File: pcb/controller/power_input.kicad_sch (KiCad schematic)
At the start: 8 parts, among them J3 USB_C_Receptacle_USB2.0_16P, U2 CH224K, U3 TPS54531DDAR

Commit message: cleaned up
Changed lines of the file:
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@@
 	(hierarchical_label "+5V"
 		(shape output)
-		(at 250.19 77.47 0)
+		(at 254 64.77 0)
 		(effects
 			(font

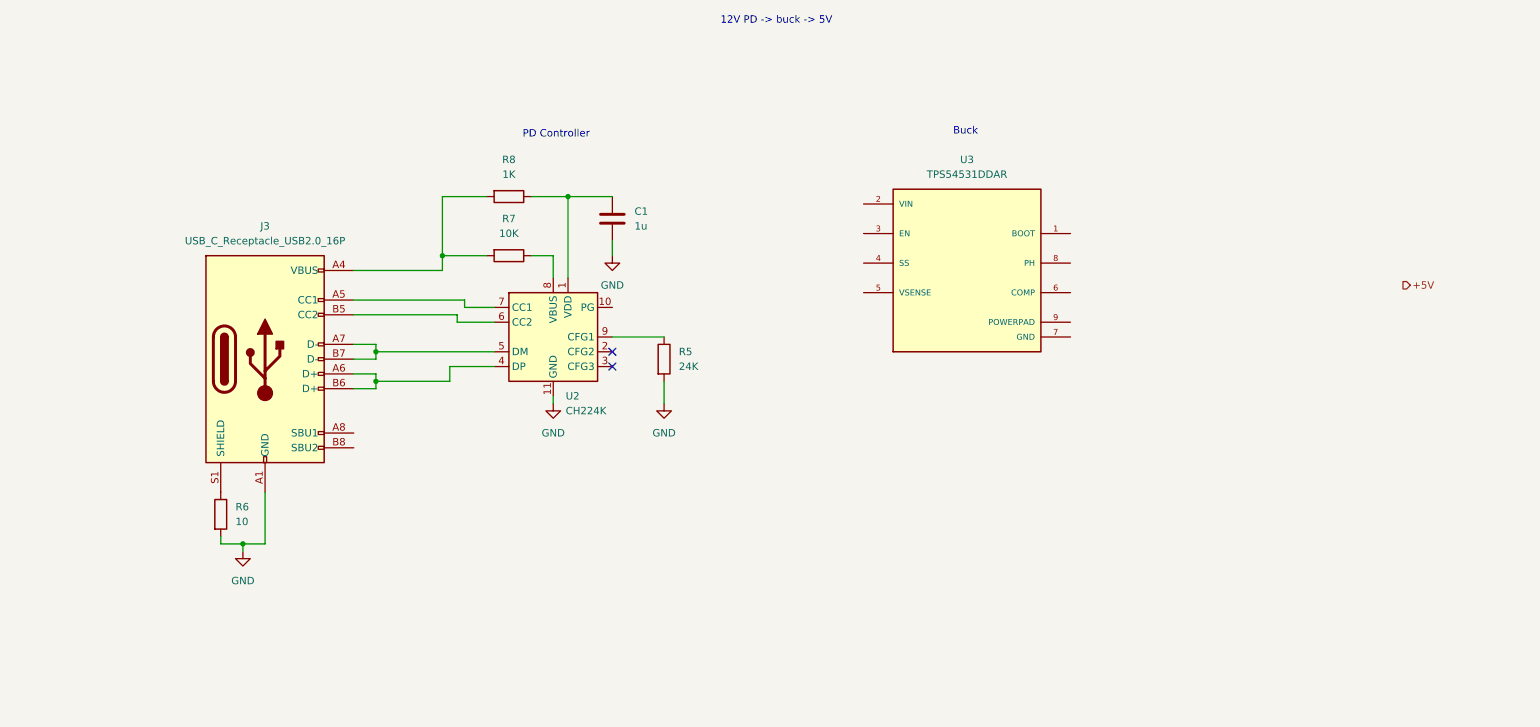
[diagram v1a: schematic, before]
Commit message: implemented PD, buck and LDO for Power Input
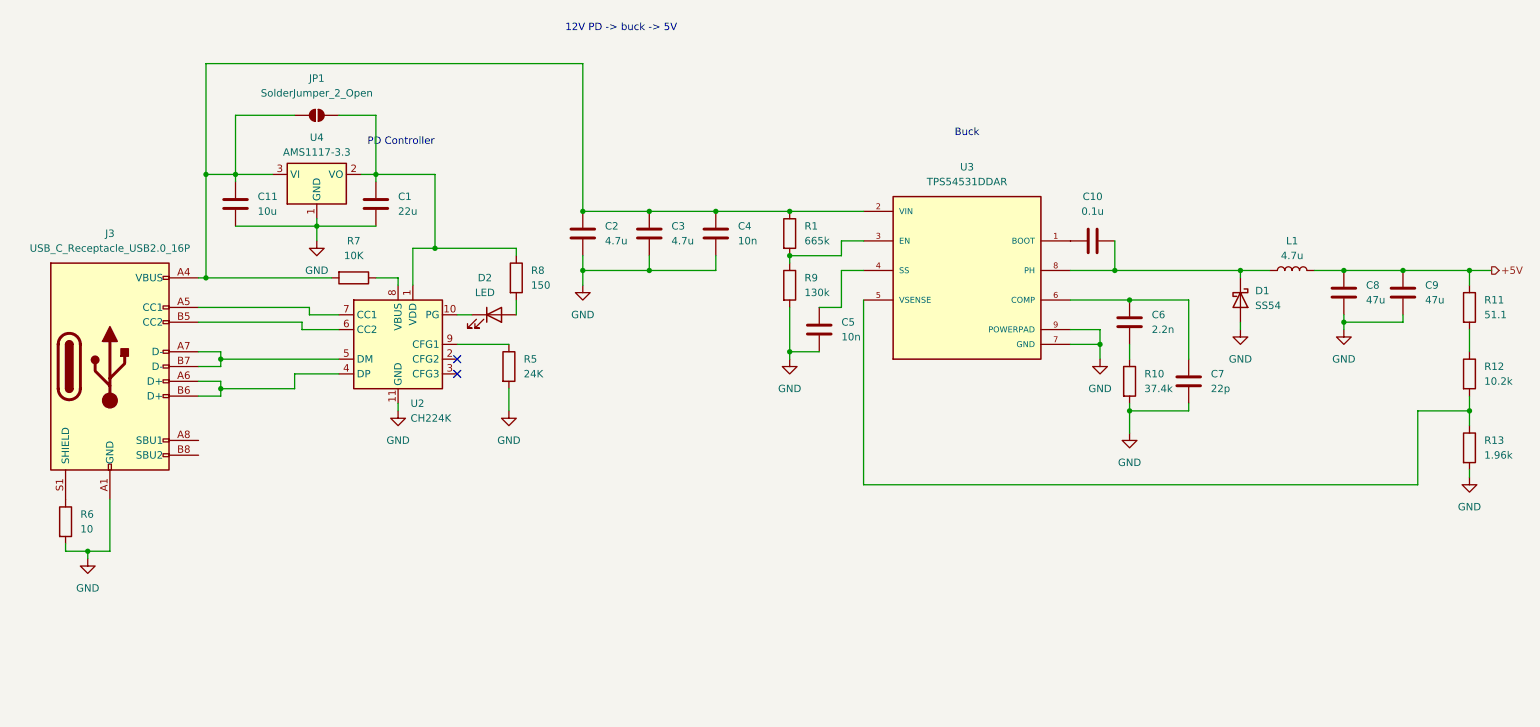
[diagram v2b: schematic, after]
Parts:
- added C10: 0.1u, symbol Device:C
- added C11: 10u, symbol Device:C
- added C2, C3: 4.7u, symbol Device:C
- added C4, C5: 10n, symbol Device:C
- added C6: 2.2n, symbol Device:C
- added C7: 22p, symbol Device:C
- added C8, C9: 47u, symbol Device:C
- added D1: SS54, symbol Device:D_Schottky
- added D2: LED, symbol Device:LED
- added JP1: SolderJumper_2_Open, Jumper:SolderJumper-2_P1.3mm_Open_TrianglePad1.0x1.5mm, symbol Jumper:SolderJumper_2_Open
- added L1: 4.7u, symbol Device:L
- added R1: 665k, symbol Device:R
- added R10: 37.4k, symbol Device:R
- added R11: 51.1, symbol Device:R
- added R12: 10.2k, symbol Device:R
- added R13: 1.96k, symbol Device:R
- added R9: 130k, symbol Device:R
- added U4: AMS1117-3.3, Package_TO_SOT_SMD:SOT-223-3_TabPin2, symbol Regulator_Linear:AMS1117-3.3
- C1: value 1u -> 22u
- R8: value 1K -> 150
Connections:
- net +5V: now also C8.1, C9.1, L1.2, R11.1
- net GND: now also U3.7 (GND), U3.9 (POWERPAD), C11.2, C2.2, C3.2, C4.2, C5.1, C7.2, C8.2, C9.2, D1.2 (A), R10.2, R13.2, R9.2, U4.1 (GND)
- net at J3.A4 (VBUS), J3.A9 (VBUS), J3.B4 (VBUS)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: now also U3.2 (VIN), C11.1, C2.1, C3.1, C4.1, JP1.2 (B), R1.1, U4.3 (VI); no longer R8.2
- net at C1.1, R8.1, U2.1 (VDD): now also JP1.1 (A), U4.2 (VO)
- net at U2.10 (PG): now also D2.1 (K)
- net at U3.1 (BOOT): now also C10.1
- net at U3.3 (EN): now also R1.2, R9.1
- net at U3.4 (SS): now also C5.2
- net at U3.5 (VSENSE): now also R12.2, R13.1
- net at U3.6 (COMP): now also C6.1, C7.1
- net at U3.8 (PH): now also C10.2, D1.1 (K), L1.1
- new net: R11.2, R12.1
- new net: D2.2 (A), R8.2
- new net: C6.2, R10.1
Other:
- moved on the sheet: C1, J3, R5, R6, R7, U2, U3

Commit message: impl eFuse
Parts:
- removed C1: 22u, symbol Device:C
- removed C10: 0.1u, symbol Device:C
- removed C11: 10u, symbol Device:C
- removed C2, C3: 4.7u, symbol Device:C
- removed C4, C5: 10n, symbol Device:C
- removed C6: 2.2n, symbol Device:C
- removed C7: 22p, symbol Device:C
- removed C8, C9: 47u, symbol Device:C
- removed D1: SS54, symbol Device:D_Schottky
- removed D2: LED, symbol Device:LED
- removed J3: USB_C_Receptacle_USB2.0_16P, symbol Connector:USB_C_Receptacle_USB2.0_16P
- removed JP1: SolderJumper_2_Open, Jumper:SolderJumper-2_P1.3mm_Open_TrianglePad1.0x1.5mm, symbol Jumper:SolderJumper_2_Open
- removed L1: 4.7u, symbol Device:L
- removed R1: 665k, symbol Device:R
- removed R10: 37.4k, symbol Device:R
- removed R11: 51.1, symbol Device:R
- removed R12: 10.2k, symbol Device:R
- removed R13: 1.96k, symbol Device:R
- removed R5: 24K, Resistor_SMD:R_0603_1608Metric, symbol Device:R
- removed R6: 10, symbol Device:R
- removed R7: 10K, symbol Device:R
- removed R8: 150, symbol Device:R
- removed R9: 130k, symbol Device:R
- removed U2: CH224K, Package_SO:SSOP-10-1EP_3.9x4.9mm_P1mm_EP2.1x3.3mm_ThermalVias, symbol Interface_USB:CH224K
- removed U3: TPS54531DDAR, TPS54531DDAR:CONV_TPS54531DDAR, symbol TPS54531DDAR:TPS54531DDAR
- removed U4: AMS1117-3.3, Package_TO_SOT_SMD:SOT-223-3_TabPin2, symbol Regulator_Linear:AMS1117-3.3
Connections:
- no-connect marks 2 -> 0
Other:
- added sheet Buck (buck.kicad_sch)
- added sheet USB-C PD (usb-c.kicad_sch)
- added sheet eFuse (efuse.kicad_sch)
- note added: "12V PD -> buck -> eFuse -> 5V"
- note removed: "12V PD -> buck -> 5V"
- note removed: "Buck"
- note removed: "PD Controller"

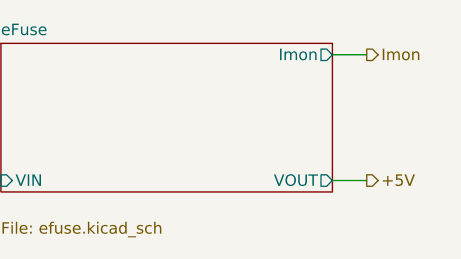
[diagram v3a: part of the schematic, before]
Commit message: added lcsc numbers to all components and added ESD protection
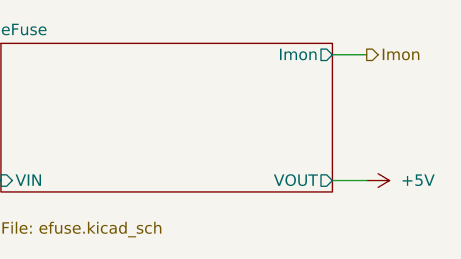
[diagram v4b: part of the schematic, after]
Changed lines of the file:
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@@
-		)
-	)
-	(hierarchical_label "+5V"
-		(shape output)
-		(at 171.45 132.08 0)
-		(effects
-			(font
-				(size 1.27 1.27)
-			)
-			(justify left)
 		)
 	)
@@
 		)
 	)
+	(symbol
+		(lib_id "power:+5V")
+		(at 171.45 132.08 270)
+		(unit 1)
+		(exclude_from_sim no)
+		(in_bom yes)
+		(on_board yes)
+		(dnp no)
+		(fields_autoplaced yes)
+		(property "Reference" "#PWR029"
+			(at 167.64 132.08 0)
+			(effects
+				(font
+					(size 1.27 1.27)
+				)
+				(hide yes)
+			)
+		)
+		(property "Value" "+5V"
+			(at 175.26 132.0799 90)
+			(effects
+				(font
+					(size 1.27 1.27)
+				)
+				(justify left)
+			)
+		)
+		(property "Footprint" ""
+			(at 171.45 132.08 0)
+			(effects
+				(font
+					(size 1.27 1.27)
+				)
+				(hide yes)
+			)
+		)
+		(property "Datasheet" ""
+			(at 171.45 132.08 0)
+			(effects
+				(font
+					(size 1.27 1.27)
+				)
+				(hide yes)
+			)
+		)
+		(property "Description" "Power symbol creates a global label with name \"+5V\""
+			(at 171.45 132.08 0)
+			(effects
+				(font
+					(size 1.27 1.27)
+				)
+				(hide yes)
+			)
+		)
+		(pin "1"
+		)
+		(instances
+			(project ""
+				(path "/c599d8cf-7937-49be-b4ed-eac09167ead4/3be86d44-1d4e-4754-862e-026f65f72643"
+					(reference "#PWR029")
+					(unit 1)
+				)
+			)
+		)
+	)
